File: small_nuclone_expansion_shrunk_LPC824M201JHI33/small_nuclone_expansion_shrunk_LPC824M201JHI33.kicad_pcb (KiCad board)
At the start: 2 copper layers, 45.8 x 25.5 mm, 5 parts, among them J1 nuclone_small_left, J2 nuclone_small_right

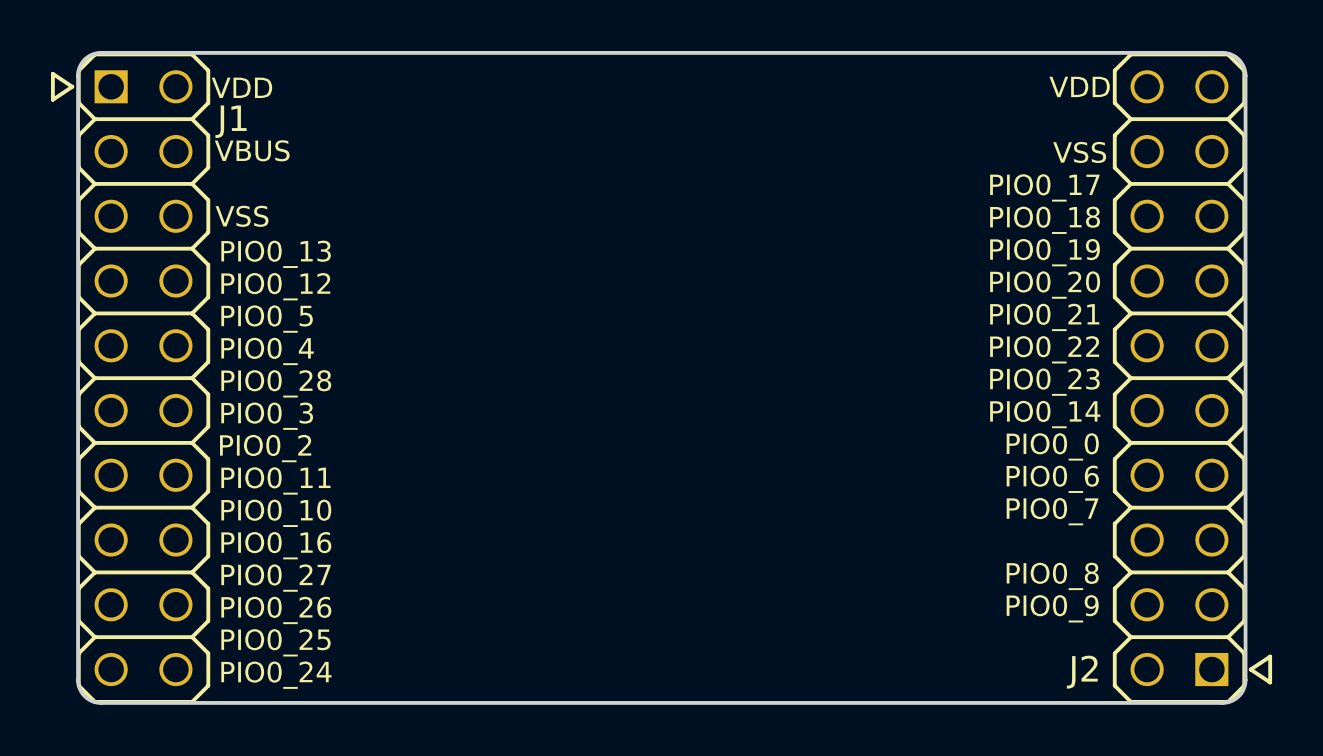
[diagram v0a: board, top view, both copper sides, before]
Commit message: updated labels
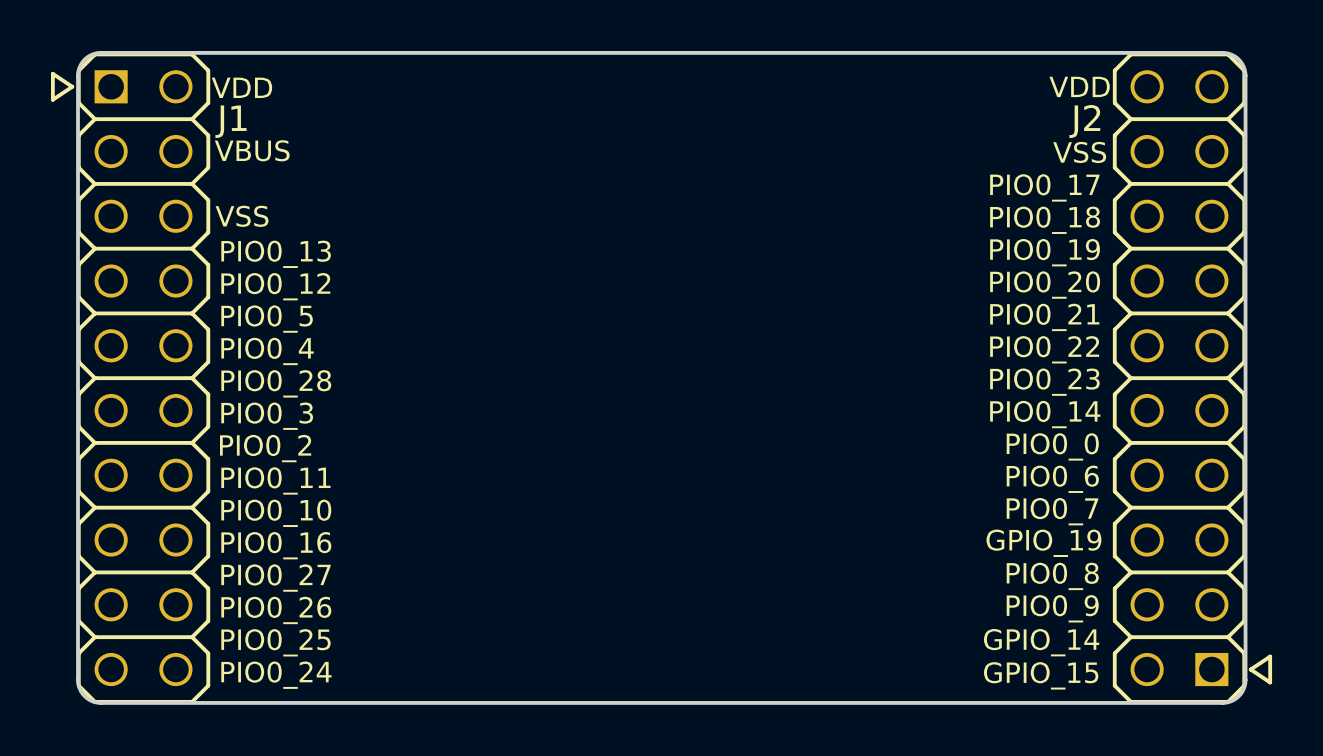
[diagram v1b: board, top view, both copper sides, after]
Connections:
- net Net-(J2-Pad1) renamed /GPIO_14
- net Net-(J2-Pad2) renamed /GPIO_15
- net Net-(J2-Pad6) renamed /GPIO_19
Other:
- board text added: "GPIO_14"
- board text added: "GPIO_15"
- board text added: "GPIO_19"
